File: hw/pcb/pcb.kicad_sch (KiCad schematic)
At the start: 66 parts, among them J1 ConnMain, J2 ConnPorts, J3 Conn_01x01_Pin, J4 Conn_01x01_Pin, J5 Conn_01x01_Pin, J6 Conn_01x01_Pin

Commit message: general progress
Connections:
- net P2_4_LV: now also D13.2 (A); no longer D15.2 (A)
- net P2_6_LV: now also D15.2 (A); no longer D13.2 (A)
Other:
- moved on the sheet: J2
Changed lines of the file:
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@@
 	)
 	(label "P1_4"
-		(at 49.53 175.26 0)
+		(at 49.53 140.97 0)
 		(fields_autoplaced yes)
 		(effects
@@
 	)
 	(label "P2_3"
-		(at 49.53 149.86 0)
+		(at 49.53 166.37 0)
 		(fields_autoplaced yes)
 		(effects
@@
 	)
 	(label "P2_2"
-		(at 49.53 152.4 0)
+		(at 49.53 163.83 0)
 		(fields_autoplaced yes)
 		(effects
@@
 	)
 	(label "P1_0"
-		(at 49.53 172.72 0)
+		(at 49.53 143.51 0)
 		(fields_autoplaced yes)
 		(effects
@@
 	)
 	(label "P2_4_LV"
-		(at 90.17 175.26 180)
+		(at 90.17 170.18 180)
 		(fields_autoplaced yes)
 		(effects
@@
 	)
 	(label "P1_2"
-		(at 49.53 167.64 0)
+		(at 49.53 148.59 0)
 		(fields_autoplaced yes)
 		(effects
@@
 	)
 	(label "P1_5"
-		(at 49.53 160.02 0)
+		(at 49.53 156.21 0)
 		(fields_autoplaced yes)
 		(effects
@@
 	)
 	(label "P2_6_LV"
-		(at 90.17 170.18 180)
+		(at 90.17 175.26 180)
 		(fields_autoplaced yes)
 		(effects
@@
 	)
 	(label "P1_3"
-		(at 49.53 165.1 0)
+		(at 49.53 151.13 0)
 		(fields_autoplaced yes)
 		(effects
@@
 	)
 	(label "P2_5"
-		(at 49.53 144.78 0)
+		(at 49.53 171.45 0)
 		(fields_autoplaced yes)
 		(effects
@@
 	)
 	(label "P2_4"
-		(at 49.53 142.24 0)
+		(at 49.53 173.99 0)
 		(fields_autoplaced yes)
 		(effects
@@
 	)
 	(label "P2_6"
-		(at 49.53 147.32 0)
+		(at 49.53 168.91 0)
 		(fields_autoplaced yes)
 		(effects
@@
 	)
 	(label "P1_1"
-		(at 49.53 170.18 0)
+		(at 49.53 146.05 0)
 		(fields_autoplaced yes)
 		(effects
@@
 	)
 	(label "P2_0"
-		(at 49.53 157.48 0)
+		(at 49.53 158.75 0)
 		(fields_autoplaced yes)
 		(effects
@@
 	)
 	(label "P1_6"
-		(at 49.53 162.56 0)
+		(at 49.53 153.67 0)
 		(fields_autoplaced yes)
 		(effects
@@
 	)
 	(label "P2_1"
-		(at 49.53 154.94 0)
+		(at 49.53 161.29 0)
 		(fields_autoplaced yes)
 		(effects
@@
 	(symbol
 		(lib_id "Connector:Conn_01x14_Pin")
-		(at 44.45 160.02 0)
-		(mirror x)
+		(at 44.45 156.21 0)
 		(unit 1)
 		(exclude_from_sim no)
@@
 		(dnp no)
 		(property "Reference" "J2"
-			(at 48.768 178.054 0)
+			(at 48.768 138.176 0)
 			(effects
 				(font
@@
 		)
 		(property "Value" "ConnPorts"
-			(at 48.514 137.922 0)
+			(at 48.514 178.308 0)
 			(effects
 				(font
@@
 		)
 		(property "Footprint" "Connector_PinHeader_2.54mm:PinHeader_1x14_P2.54mm_Horizontal"
-			(at 44.45 160.02 0)
+			(at 44.45 156.21 0)
 			(effects
 				(font
@@
 		)
 		(property "Datasheet" "~"
-			(at 44.45 160.02 0)
+			(at 44.45 156.21 0)
 			(effects
 				(font
@@
 		)
 		(property "Description" "Generic connector, single row, 01x14, script generated"
-			(at 44.45 160.02 0)
+			(at 44.45 156.21 0)
 			(effects
 				(font

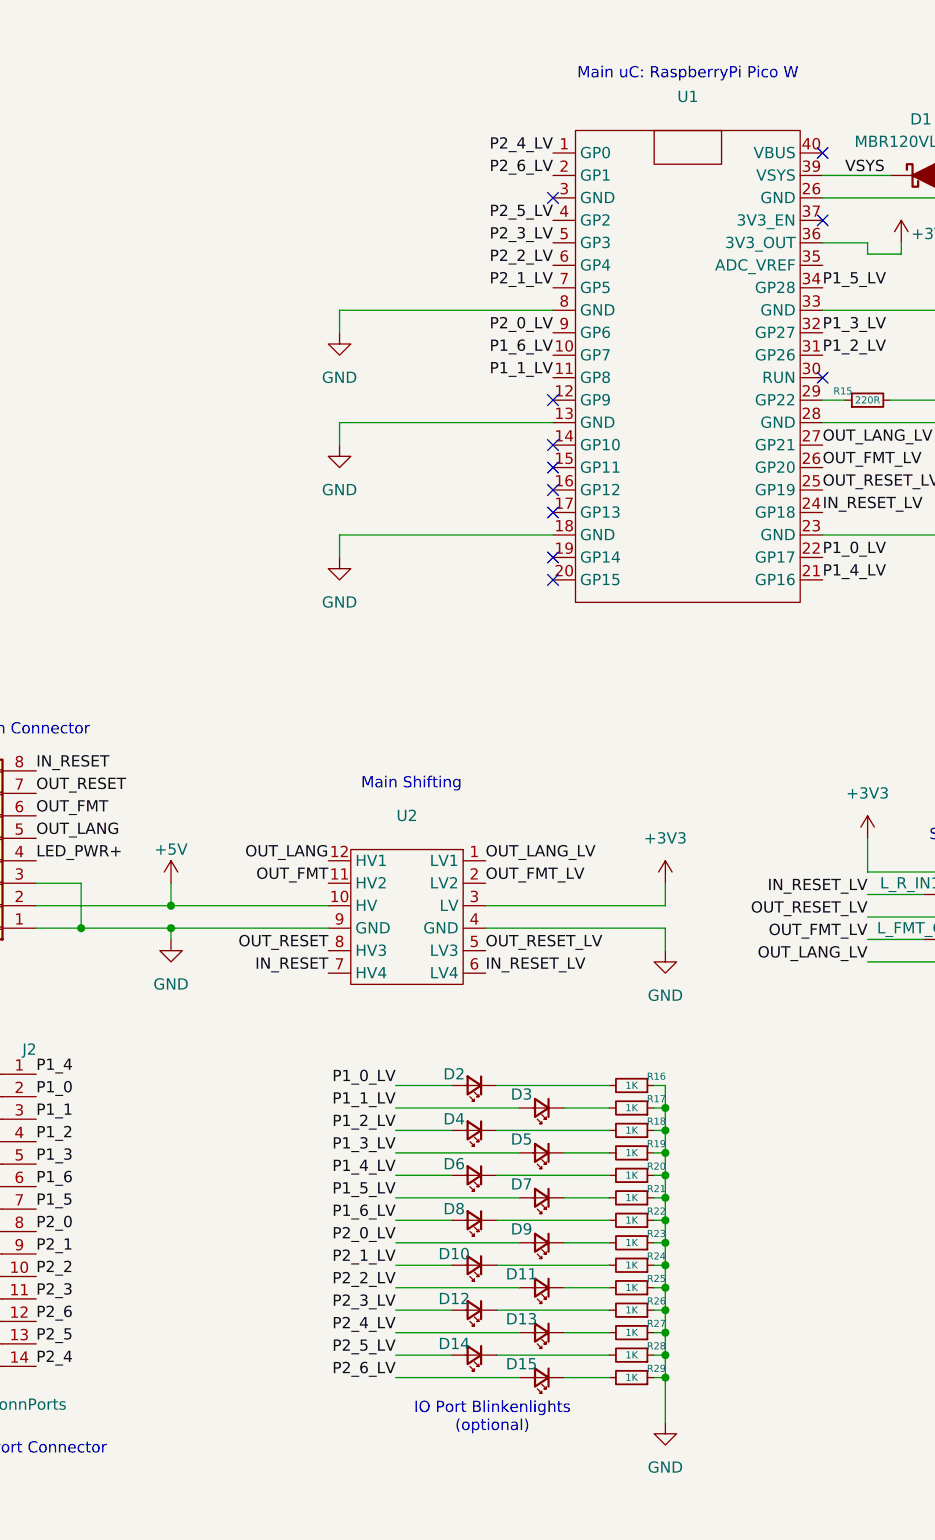
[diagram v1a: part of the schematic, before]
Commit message: changed to use gpio irqs for fast response in port code, general changes
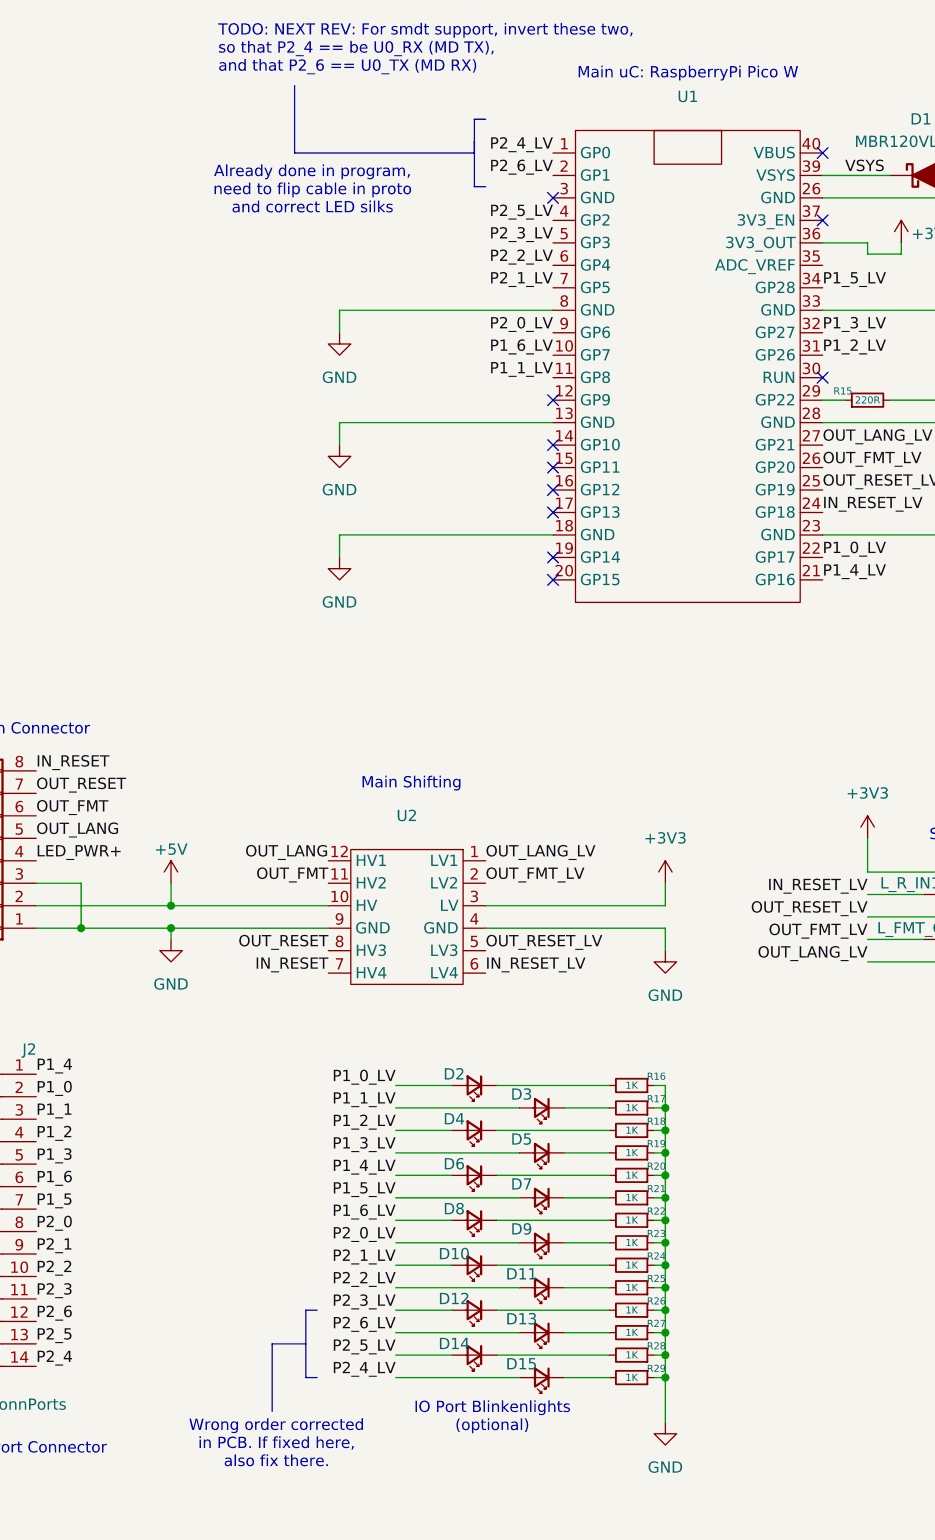
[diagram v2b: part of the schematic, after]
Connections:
- net P2_4_LV: now also D15.2 (A); no longer D13.2 (A)
- net P2_6_LV: now also D13.2 (A); no longer D15.2 (A)
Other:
- note added: "Already done in program, need to flip cable in proto and correct LED silks"
- note added: "TODO: NEXT REV: For smdt support, invert these two, so that P2_4 == be U0_RX (MD TX), and that P2_6 == U0_TX (MD RX)"
- note added: "Wrong order corrected in PCB. If fixed here, also fix there."
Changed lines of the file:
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@@
+		)
+	)
+	(polyline
+		(pts
+			(xy 80.01 167.64) (xy 80.01 175.26)
+		)
+		(stroke
+			(width 0)
+			(type default)
 		)
 	)
@@
 		)
 	)
+	(polyline
+		(pts
+			(xy 99.06 35.56) (xy 99.06 33.02)
+		)
+		(stroke
+			(width 0)
+			(type default)
+		)
+	)
 	(wire
 		(pts
@@
 		)
 	)
+	(polyline
+		(pts
+			(xy 99.06 35.56) (xy 99.06 40.64)
+		)
+		(stroke
+			(width 0)
+			(type default)
+		)
+	)
 	(wire
 		(pts
@@
 		)
 	)
+	(polyline
+		(pts
+			(xy 80.01 175.26) (xy 81.28 175.26)
+		)
+		(stroke
+			(width 0)
+			(type default)
+		)
+	)
 	(wire
 		(pts
@@
 		)
 	)
+	(polyline
+		(pts
+			(xy 76.2 171.45) (xy 76.2 179.07)
+		)
+		(stroke
+			(width 0)
+			(type default)
+		)
+	)
 	(wire
 		(pts
@@
 		)
 	)
+	(polyline
+		(pts
+			(xy 99.06 33.02) (xy 100.33 33.02)
+		)
+		(stroke
+			(width 0)
+			(type default)
+		)
+	)
 	(wire
 		(pts
@@
 		)
 	)
+	(polyline
+		(pts
+			(xy 78.74 29.21) (xy 78.74 36.83)
+		)
+		(stroke
+			(width 0)
+			(type default)
+		)
+	)
 	(wire
 		(pts
@@
 		)
 	)
+	(polyline
+		(pts
+			(xy 78.74 36.83) (xy 99.06 36.83)
+		)
+		(stroke
+			(width 0)
+			(type default)
+		)
+	)
 	(wire
 		(pts
@@
 		)
 	)
+	(polyline
+		(pts
+			(xy 99.06 35.56) (xy 99.06 36.83)
+		)
+		(stroke
+			(width 0)
+			(type default)
+		)
+	)
 	(wire
 		(pts
@@
 		)
 	)
+	(polyline
+		(pts
+			(xy 81.28 167.64) (xy 80.01 167.64)
+		)
+		(stroke
+			(width 0)
+			(type default)
+		)
+	)
 	(wire
 		(pts
@@
 		)
 	)
+	(polyline
+		(pts
+			(xy 99.06 40.64) (xy 100.33 40.64)
+		)
+		(stroke
+			(width 0)
+			(type default)
+		)
+	)
 	(wire
 		(pts
@@
 		(pts
 			(xy 199.39 76.2) (xy 213.36 76.2)
+		)
+		(stroke
+			(width 0)
+			(type default)
+		)
+	)
+	(polyline
+		(pts
+			(xy 80.01 171.45) (xy 76.2 171.45)
 		)
 		(stroke
@@
 		)
 	)
+	(text "Wrong order corrected\nin PCB. If fixed here,\nalso fix there."
+		(exclude_from_sim no)
+		(at 76.708 182.88 0)
+		(effects
+			(font
+				(size 1.27 1.27)
+			)
+		)
+	)
 	(text "IO Port Blinkenlights\n(optional)"
 		(exclude_from_sim no)
@@
 		)
 	)
+	(text "TODO: NEXT REV: For smdt support, invert these two,\nso that P2_4 == be U0_RX (MD TX),\nand that P2_6 == U0_TX (MD RX)"
+		(exclude_from_sim no)
+		(at 70.104 25.146 0)
+		(effects
+			(font
+				(size 1.27 1.27)
+			)
+			(justify left)
+		)
+	)
+	(text "Already done in program,\nneed to flip cable in proto\nand correct LED silks"
+		(exclude_from_sim no)
+		(at 80.772 41.148 0)
+		(effects
+			(font
+				(size 1.27 1.27)
+			)
+		)
+	)
 	(text "Port 1 Shifting"
 		(exclude_from_sim no)
@@
 	)
 	(label "P2_4_LV"
-		(at 90.17 170.18 180)
+		(at 90.17 175.26 180)
 		(fields_autoplaced yes)
 		(effects
@@
 	)
 	(label "P2_6_LV"
-		(at 90.17 175.26 180)
-		(fields_autoplaced yes)
-		(effects
+		(at 90.17 170.18 180)
+		(fields_autoplaced yes)
+		(effects

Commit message: [hw] initial v3 design, updated readme
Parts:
- removed J3, J4, J5, J6: Conn_01x01_Pin, Connector_PinHeader_2.54mm:PinHeader_1x01_P2.54mm_Vertical, symbol Connector:Conn_01x01_Pin
- removed U2, U3, U4, U5, U6: ~, footprints:cheap_lvl_shifter_4ch, symbol modules:lvl_shifter
- added R35, R36, R37: 1K, Resistor_SMD:R_0805_2012Metric_Pad1.20x1.40mm_HandSolder, symbol Device:R_Small
- added U2, U3, U4: TXS0108EPW, Package_SO:TSSOP-20_4.4x6.5mm_P0.65mm, symbol Logic_LevelTranslator:TXS0108EPW
- J2: footprint Connector_PinHeader_2.54mm:PinHeader_1x14_P2.54mm_Horizontal -> Connector_PinHeader_2.54mm:PinHeader_1x14_P2.54mm_Vertical
- R1, R10, R11, R12, R13, R14, R2, R3, R4, R5, R6, R7, R8, R9: value 10K -> 1K
- U1: footprint Module_RaspberryPi_Pico:RaspberryPi_Pico_W_SMD_MountingHoles_Castellated_HandSolder -> Module:RaspberryPi_Pico_W_SMD_HandSolder; symbol modules:pico_w -> MCU_Module:RaspberryPi_Pico_W
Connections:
- net +3V3: now also R37.2, U2.2 (VCCA), U3.2 (VCCA), U4.2 (VCCA)
- net +5V: now also U2.19 (VCCB), U3.19 (VCCB), U4.19 (VCCB)
- net GND: now also U1.3 (GND), U1.38 (GND), R35.1, R36.1, U2.11 (GND), U3.11 (GND), U4.11 (GND); no longer U1.26 (GP20)
- net IN_RESET: now also U4.12 (B8)
- net IN_RESET_LV: now also U1.22 (GPIO17), U4.9 (A8); no longer U1.24 (GP18)
- net OUT_FMT: now also U4.14 (B6)
- net OUT_FMT_LV: now also U1.25 (GPIO19), U4.7 (A6); no longer U1.26 (GP20)
- net OUT_LANG: now also U4.15 (B5)
- net OUT_LANG_LV: now also U1.24 (GPIO18), U4.6 (A5); no longer U1.27 (GP21)
- net OUT_RESET: now also U4.13 (B7)
- net OUT_RESET_LV: now also U1.21 (GPIO16), U4.8 (A7); no longer U1.25 (GP19)
- net P1_0_LV: now also U1.1 (GPIO0), U2.3 (A2); no longer U1.22 (GP17)
- net P1_1_LV: now also U1.2 (GPIO1), U2.4 (A3); no longer U1.11 (GP8)
- net P1_2_LV: now also U1.4 (GPIO2), U2.5 (A4); no longer U1.31 (GP26)
- net P1_3_LV: now also U1.5 (GPIO3), U2.6 (A5); no longer U1.32 (GP27)
- net P1_4_LV: now also U1.7 (GPIO5), U2.1 (A1); no longer U1.21 (GP16)
- net P1_5: now also J2.6 (Pin_6), R6.2; no longer J2.7 (Pin_7), R7.2
- net P1_5_LV: now also U1.6 (GPIO4), U2.7 (A6); no longer U1.34 (GP28)
- net P1_6: now also J2.7 (Pin_7), R7.2; no longer J2.6 (Pin_6), R6.2
- net P1_6_LV: now also U1.9 (GPIO6), U2.8 (A7); no longer U1.10 (GP7)
- net P2_0_LV: now also U1.11 (GPIO8), U3.1 (A1); no longer U1.9 (GP6)
- net P2_1_LV: now also U1.12 (GPIO9), U3.3 (A2); no longer U1.7 (GP5)
- net P2_2_LV: now also U1.14 (GPIO10), U3.4 (A3); no longer U1.6 (GP4)
- net P2_3_LV: now also U1.15 (GPIO11), U3.5 (A4); no longer U1.5 (GP3)
- net P2_4_LV: now also D13.2 (A), U1.17 (GPIO13), U3.8 (A7); no longer D15.2 (A), U1.1 (GP0)
- net P2_5: now also J2.12 (Pin_12), R12.2; no longer J2.13 (Pin_13), R13.2
- net P2_5_LV: now also U1.16 (GPIO12), U3.6 (A5); no longer U1.4 (GP2)
- net P2_6: now also J2.13 (Pin_13), R13.2; no longer J2.12 (Pin_12), R12.2
- net P2_6_LV: now also D15.2 (A), U1.19 (GPIO14), U3.7 (A6); no longer D13.2 (A), U1.2 (GP1)
- net at R6.1: now also U2.14 (B6)
- net at R8.1: now also U3.20 (B1)
- net at R12.1: now also U3.15 (B5)
- net at R10.1: now also U3.17 (B3)
- net at R9.1: now also U3.18 (B2)
- net at R7.1: now also U2.13 (B7)
- net at R14.1: now also U3.13 (B7)
- net at R4.1: now also U2.16 (B4)
- net at R5.1: now also U2.15 (B5)
- net at R3.1: now also U2.17 (B3)
- net at R15.1: now also U1.32 (GPIO27_ADC1); no longer U1.29 (GP22)
- net at R13.1: now also U3.14 (B6)
- net at R11.1: now also U3.16 (B4)
- net at R1.1: now also U2.20 (B1)
- net at R2.1: now also U2.18 (B2)
- net P2_OE: now reaches U1.20 (GPIO15)
- net P2_OE: now also R35.2, U3.10 (OE)
- new net: R37.1, U4.10 (OE)
- new net P1_OE: R36.2, U1.10 (GPIO7), U2.10 (OE)
- no-connect marks 11 -> 21
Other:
- note added: "CONNECTORS"
- note added: "LEDs"
- note added: "LEVEL SHIFTERS"
- note added: "PICO W"
- note removed: "Already done in program, need to flip cable in proto and correct LED silks"
- note removed: "Main Shifting"
- note removed: "Main uC: RaspberryPi Pico W"
- note removed: "Port 1 Shifting"
- note removed: "Port 2 Shifting"
- note removed: "TODO: NEXT REV: For smdt support, invert these two, so that P2_4 == be U0_RX (MD TX), and that P2_6 == U0_TX (MD RX)"
- note removed: "Wrong order corrected in PCB. If fixed here, also fix there."
- moved on the sheet: D1, D10, D11, D12, D13, D14, D15, D2, D3, D4, D5, D6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

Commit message: [hw] final tweaks for pcb, incl. fabrication files
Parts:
- added H1, H2, H3, H4: MountingHole, MountingHole:MountingHole_2.2mm_M2_ISO14580, symbol Mechanical:MountingHole
- D1: LCSC PN (none) -> C223608
- D10, D11, D12, D13, D14, D15, D2, D3, D4, D5, D6, D7, D8, D9: LCSC PN (none) -> C965813
- J1: LCSC PN (none) -> C492416
- J2: LCSC PN (none) -> C18905874
- L_FMT_OUT1, L_LANG_OUT1, L_R_IN1, L_R_OUT1: LCSC PN (none) -> C965817
- L_PWR1: LCSC PN (none) -> C965812
- R1, R10, R11, R12, R13, R14, R16, R17, R18, R19, R2, R20, R21, R22, R23, R24, R25, R26, R27, R28, R29, R3, R30, R31, R32, R33, R34, R35, R36, R37, R4, R5, R6, R7, R8, R9: LCSC PN (none) -> C17513
- R15: LCSC PN (none) -> C114519
- U1: LCSC PN (none) -> C7203003
- U2, U3, U4: LCSC PN (none) -> C17206
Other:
- note added: "MOUNTING, MISC."
- note removed: "1"
- note removed: "mega-paladin v2"
- company: (none) -> camargo.eng.br
- title: (none) -> mega-paladin v3
- moved on the sheet: D1, R15, U1
